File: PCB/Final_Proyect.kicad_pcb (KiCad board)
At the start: 2 copper layers, 76 x 44.5 mm, 89 parts, among them J1 Conn_01x10_Pin, J2 VCC GND TTP223, J3 OLLED I2C, J4 - +, J5 USB_C, U1 ESP32-S3-WROOM-1, U2 AMS1117-3.3, U3 DRV8870DDA, U4 DRV8870DDA, U5 DRV8870DDA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

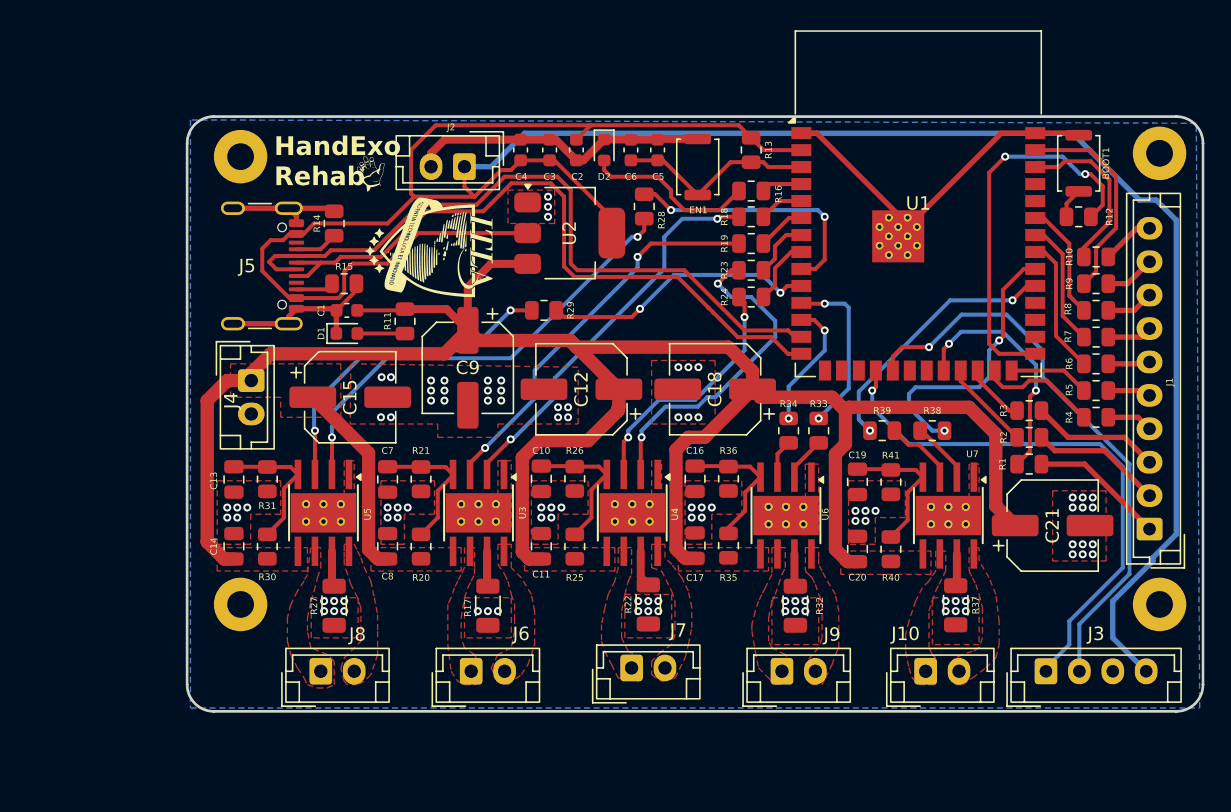
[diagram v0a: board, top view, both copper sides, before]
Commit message: Enrutamiento mejorado
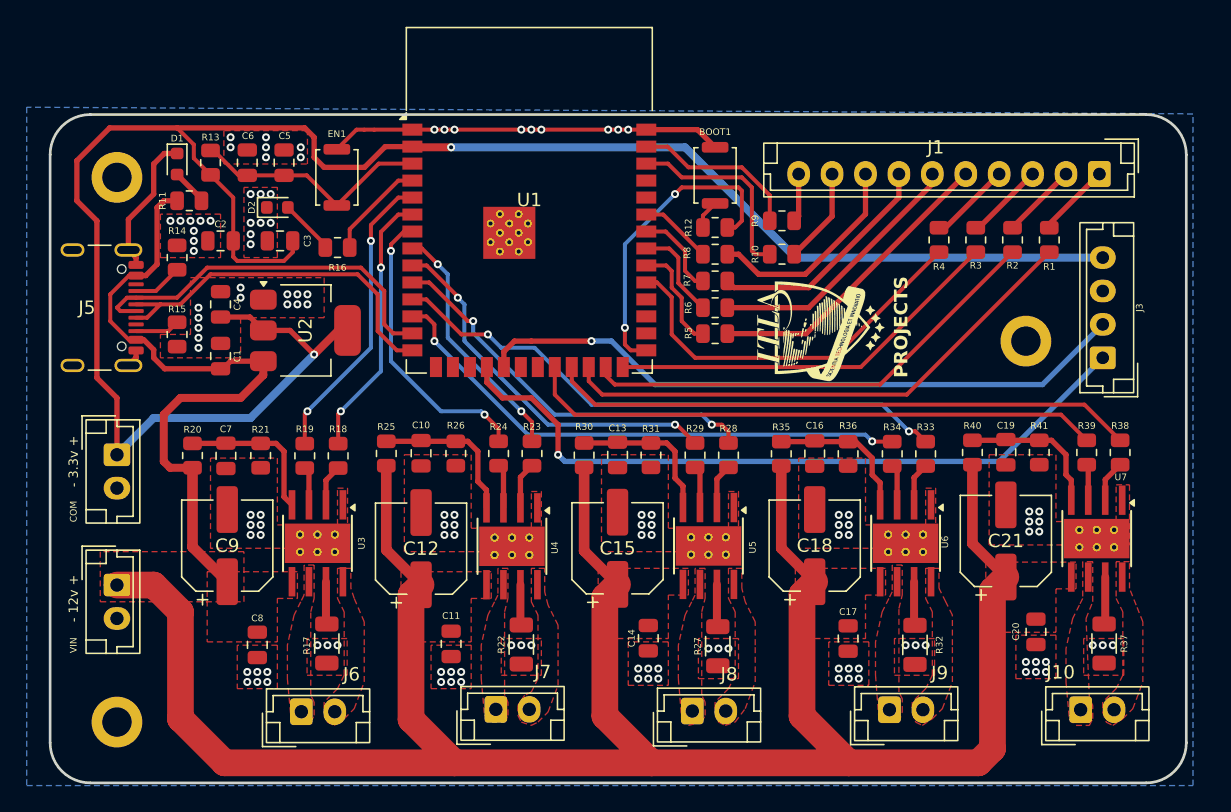
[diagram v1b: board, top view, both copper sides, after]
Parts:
- removed the ? at (180.8, 85.5)
- removed the ? at (180.8, 119.2)
- removed the ? at (112.0, 119.2)
- removed the ? at (112.0, 85.7)
- removed the G*** at (121.8, 87.0)
- added ?: , , F.Cu at (170.8, 99.5)
- added ?: , , F.Cu at (102.8, 128.0)
- added REF**: MountingHole_2.2mm_M2_DIN965_Pad, MountingHole:MountingHole_2.2mm_M2_DIN965_Pad, F.Cu at (102.8, 87.2)
- - 12v +: renamed from J4
- - 3.3v +: renamed from J2
- C1, C2, C4, C5: footprint Capacitor_SMD:C_0603_1608Metric -> Capacitor_SMD:C_0805_2012Metric
- C10, C11, C13, C14, C16, C17, C19, C20, C7, C8: value C -> 100nF
- C12, C15, C18, C21, C9: value C_Polarized -> 47uF; footprint Capacitor_SMD:CP_Elec_6.3x5.4 -> Capacitor_SMD:CP_Elec_6.3x7.7
- C3, C6: value 100uf -> 100nf; footprint Capacitor_SMD:C_0603_1608Metric -> Capacitor_SMD:C_0805_2012Metric
- R1, R10, R2, R3, R4, R5, R6, R7, R8, R9: value 470 -> 1k
- R17, R22, R27, R32, R37: value R -> 0.2
- R18, R19, R23, R24, R28, R29, R33, R34, R38, R39: value R -> 1k
- R20, R25, R30, R35, R40: value R -> 80k
- R21, R26, R31, R36, R41: value R -> 10k
- moved R13 40.5 mm to (109.8, 86.2), turned to 90 degrees
- moved R19 37.0 mm to (116.8, 108.1), turned to 90 degrees
- moved R18 35.7 mm to (119.3, 108.1), turned to -90 degrees
- moved - 3.3v + 33.8 mm to (102.8, 108.0), turned to -90 degrees
- moved C14 31.8 mm to (142.5, 121.7), turned to -90 degrees
- moved R16 31.2 mm to (119.2, 92.5)
- moved G*** 30.6 mm to (155.8, 98.8), turned to 90 degrees
- moved U1 29.1 mm to (133.6, 88.9)
- moved U5 28.9 mm to (147.0, 114.8)
- moved R27 28.9 mm to (147.7, 122.3)
- moved R5 28.8 mm to (147.5, 98.9)
- moved R6 28.8 mm to (147.5, 97.0)
- moved R7 28.8 mm to (147.5, 95.0)
- moved R8 28.8 mm to (147.5, 93.0)
- moved C13 28.8 mm to (140.2, 108.0)
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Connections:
- J5 pad A4: +3V3 -> +12V
- J5 pad A9: +3V3 -> +12V
- J5 pad B4: +3V3 -> +12V
- J5 pad B9: +3V3 -> +12V
- R10 pad 1: Net-(J1-Pin_10) -> Net-(J1-Pin_9)
- R9 pad 1: Net-(J1-Pin_9) -> Net-(J1-Pin_10)
- U1 pad 10: C- -> C+
- U1 pad 22: SIG10 -> F-
- U1 pad 23: SIG9 -> F+
- U1 pad 24: SIG8 -> SIG10
- U1 pad 25: SIG7 -> SIG9
- U1 pad 26: SIG6 -> SIG8
- U1 pad 31: F- -> SIG7
- U1 pad 32: F+ -> SIG6
- U1 pad 5: A+ -> A-
- U1 pad 6: A- -> A+
- U1 pad 7: B+ -> B-
- U1 pad 8: B- -> B+
- U1 pad 9: C+ -> C-
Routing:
- net +12V: track 172.1 -> 225.1 mm
- net +3V3: track 189.2 -> 153.5 mm, vias 0 -> 2
- net GND: track 73.4 -> 41.5 mm, vias 93 -> 120
- net /Motor Driver2/IN2: track 34.5 -> 3.36 mm, vias 2 -> 0
- net E-: track 9.78 -> 40.5 mm
- net E+: track 12.9 -> 42.8 mm
- net SIG9: track 6.74 -> 35.5 mm
- net /Motor Driver/IN1: track 29.5 -> 2.89 mm, vias 2 -> 0
- net /Motor Driver/IN2: track 29.6 -> 3.13 mm, vias 2 -> 0
- net SIG8: track 4.56 -> 30.0 mm
- net D-: track 52.4 -> 28.4 mm
- net F-: track 19.7 -> 43.3 mm, vias 2 -> 0
- net D+: track 50.8 -> 27.8 mm
- net F+: track 20.9 -> 43.9 mm, vias 2 -> 0
- net SIG10: track 18.7 -> 40.3 mm, vias 2 -> 0
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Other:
- board size 76 x 44.5 mm -> 85 x 50 mm
- board text added: "COM"
- board text added: "PROJECTS"
- board text added: "VIN"
- board text removed: "HandExo Rehab"

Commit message: Finalizado
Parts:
- added C22: 220uF, Capacitor_SMD:CP_Elec_6.3x7.7, F.Cu at (110.8, 106.2)
- added C23: 100nf, Capacitor_SMD:C_0805_2012Metric, F.Cu at (118.2, 86.2)
- added D3: SS18, Diode_SMD:D_SMA, F.Cu at (106.5, 121.5)
- added G***: LOGO, Images:Logo_Mano, F.Cu at (171.2, 102.5)
- moved BOOT 49.4 mm to (101.5, 105.0), turned to 180 degrees
- moved R12 41.8 mm to (106.0, 86.1), turned to 90 degrees
- moved R3 18.9 mm to (150.0, 100.2), turned to 180 degrees
- moved EN 18.0 mm to (101.5, 90.5), turned to 180 degrees
- moved ? 15.6 mm to (179.0, 86.2)
- moved R4 13.0 mm to (154.2, 100.2), turned to 180 degrees
- moved R20 12.6 mm to (120.2, 103.8), turned to 180 degrees
- moved C4 11.8 mm to (115.8, 86.2)
- moved C2 11.8 mm to (120.8, 86.2), turned to 90 degrees
- moved R2 11.5 mm to (161.8, 100.2), turned to 180 degrees
- moved R1 9.58 mm to (167.8, 100.2), turned to 180 degrees
- moved G*** 9.52 mm to (164.5, 95.0), turned to 0 degrees
- moved R7 8.62 mm to (155.0, 90.8), turned to -90 degrees
- moved C5 7.99 mm to (108.2, 90.0), turned to -90 degrees
- moved D1 7.63 mm to (112.0, 92.2), turned to 180 degrees
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- renumbered BOOT1 to BOOT, EN1 to EN
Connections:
- - 12v + pad 1: +12V -> Net-(D3-A)
- ? pad 1: (no net) -> GND (x2)
- REF** pad 1: (no net) -> GND
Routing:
- net GND: track 41.5 -> 99.4 mm, vias 120 -> 101
- net +3V3: track 153.5 -> 118.1 mm, vias 2 -> 5
- net BOOT: track 23.4 -> 49.1 mm
- net SIG8: track 30.0 -> 9.00 mm
- net Net-(BOOT1-A): track 2.18 -> 22.5 mm
- net Net-(J1-Pin_3): track 6.41 -> 24.7 mm
- net SIG7: track 29.1 -> 13.1 mm
- net Net-(J1-Pin_7): track 17.6 -> 3.75 mm
- net SIG9: track 35.5 -> 23.5 mm
- net Net-(J1-Pin_8): track 15.8 -> 3.86 mm
- net Net-(J1-Pin_4): track 6.16 -> 17.2 mm
- net Net-(J1-Pin_2): track 5.67 -> 16.2 mm
- net Net-(J1-Pin_6): track 20.4 -> 10.1 mm
- net EN: track 18.1 -> 27.8 mm
- net +12V: track 225.1 -> 234.8 mm
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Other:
- board text added: "HandExo-Rehab"
- board text removed: "PROJECTS"
